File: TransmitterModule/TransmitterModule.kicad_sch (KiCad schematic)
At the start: 22 parts, among them J3 Battery, U1 NRF24L01_, U3 102010388, U4 LD1086DTTR

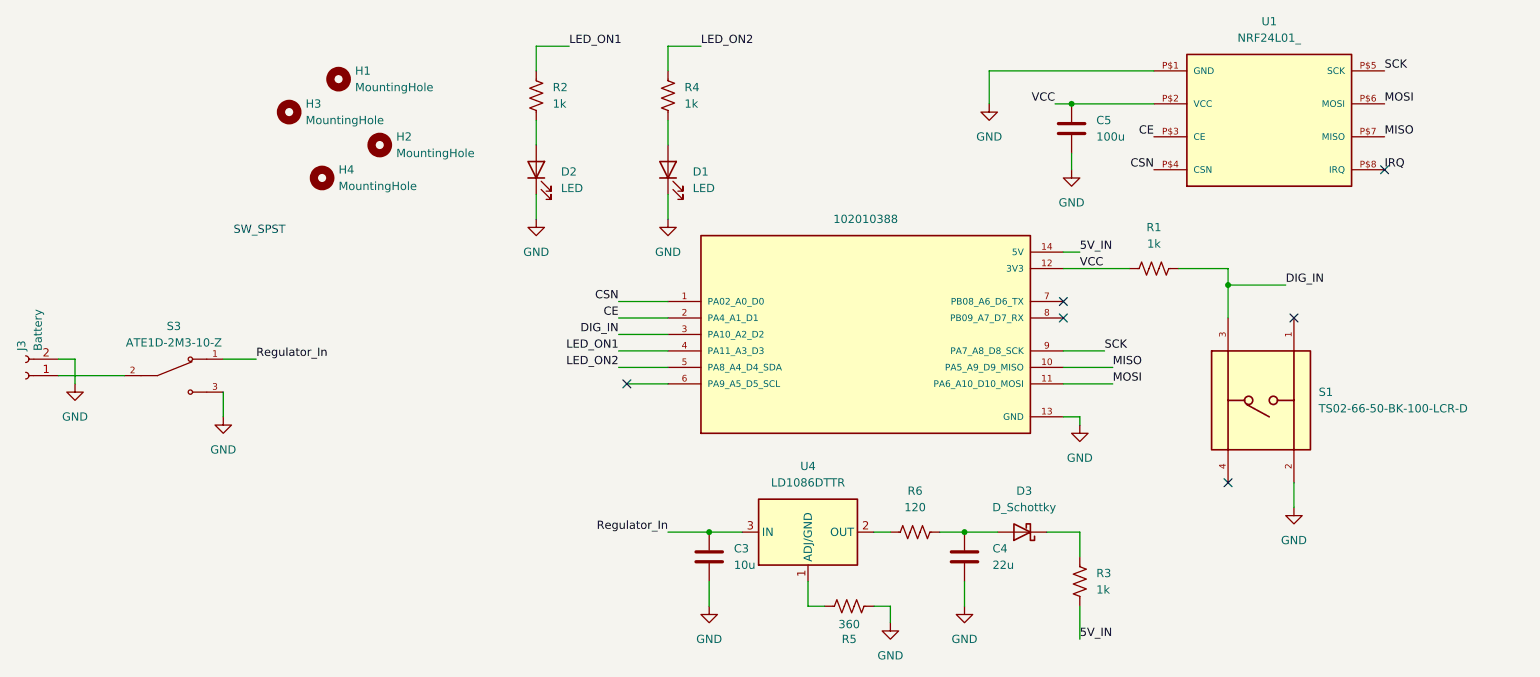
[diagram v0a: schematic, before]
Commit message: updated transmitter module to delete LOD and change button layout
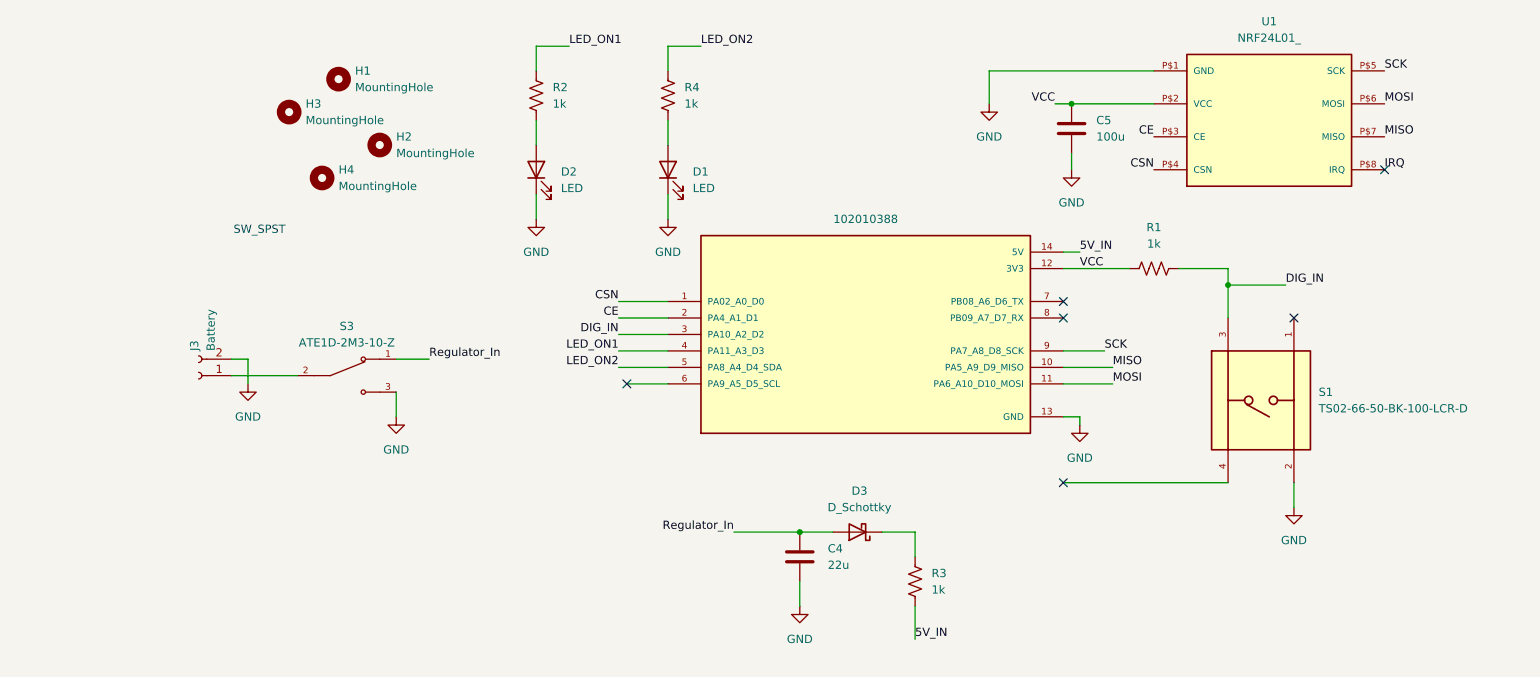
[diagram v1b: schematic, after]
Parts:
- removed C3: 10u, Capacitor_THT:C_Axial_L3.8mm_D2.6mm_P7.50mm_Horizontal, symbol Device:C
- removed R5: 360, Resistor_THT:R_Axial_DIN0204_L3.6mm_D1.6mm_P2.54mm_Vertical, symbol Device:R_US
- removed R6: 120, Resistor_THT:R_Axial_DIN0204_L3.6mm_D1.6mm_P2.54mm_Vertical, symbol Device:R_US
- removed U4: LD1086DTTR, Package_TO_SOT_SMD:TO-252-2, symbol Regulator_Linear:LD1086DTTR
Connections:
- net Regulator_In: now also C4.1, D3.2 (A)
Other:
- moved on the sheet: C4, D3, J3, R3, S3
